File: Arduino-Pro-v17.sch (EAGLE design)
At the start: 39 parts, among them IC1 ATMEGA1281-16AU, IC2 MCP170312MB, J1 FTDI Basic Programmer

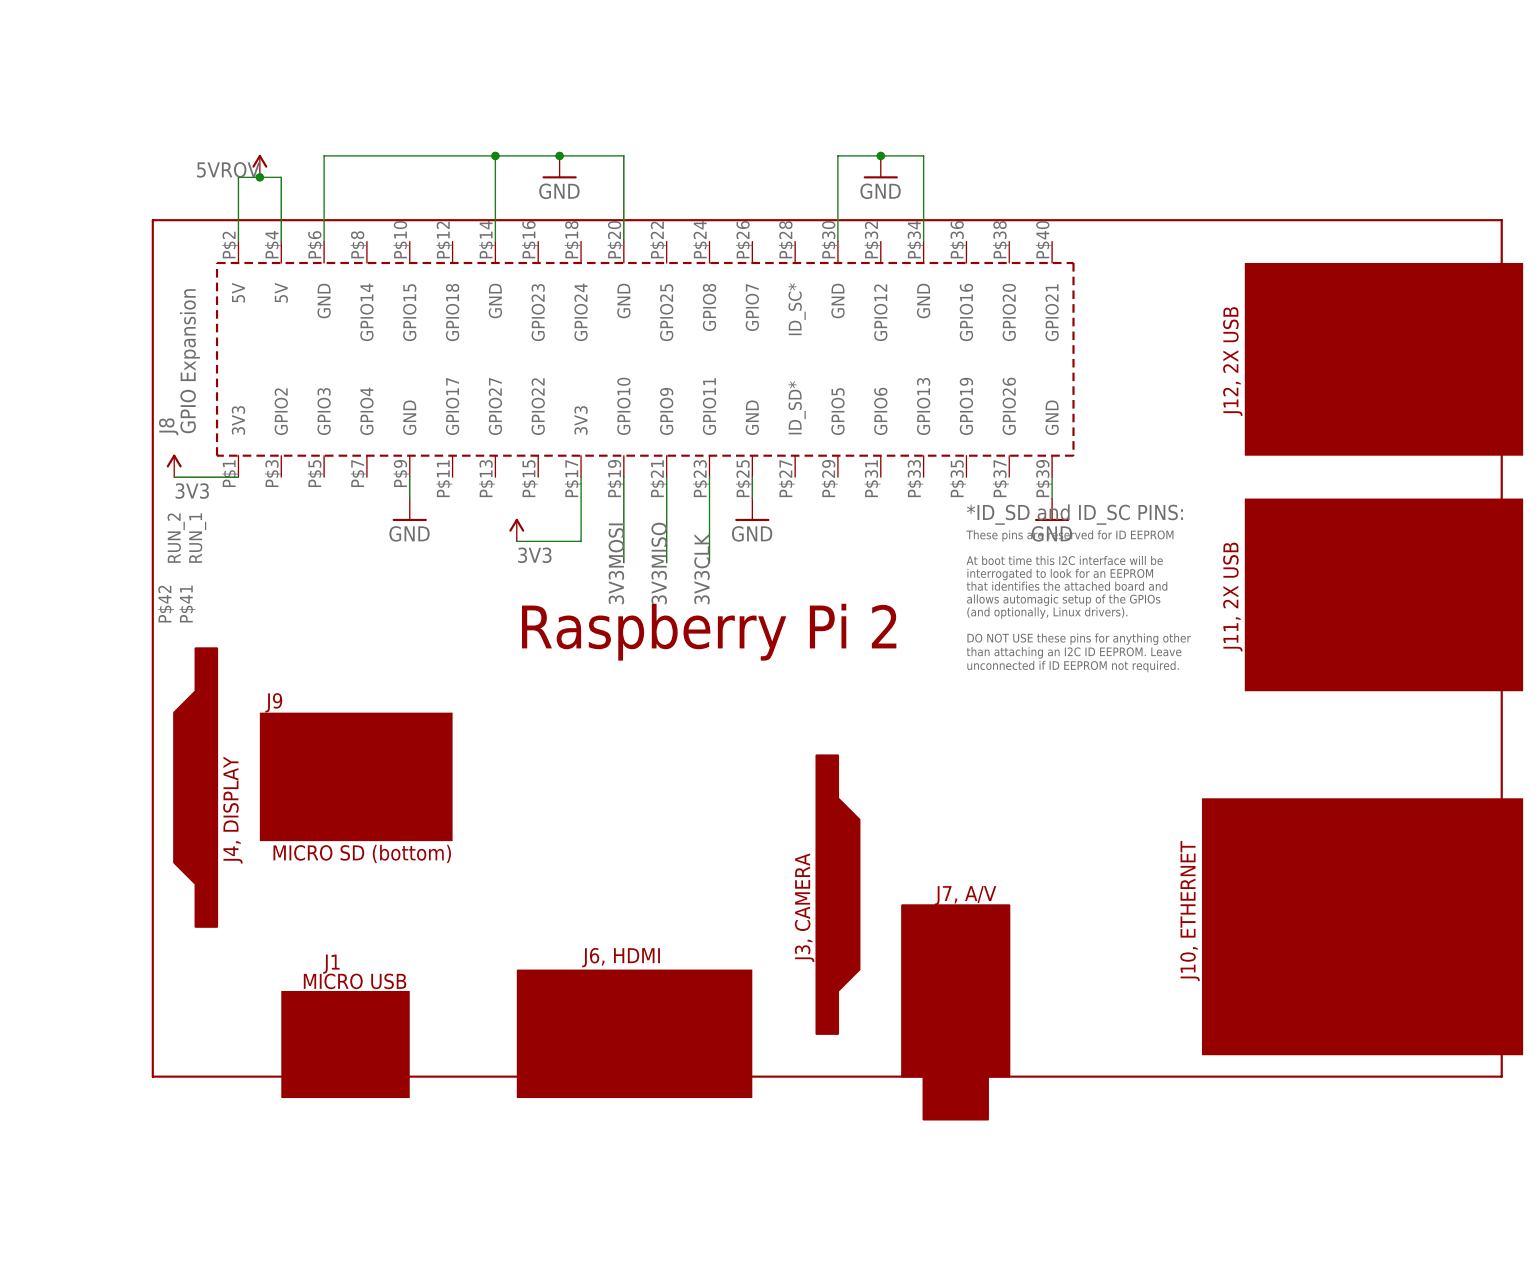
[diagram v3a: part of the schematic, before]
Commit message: Removed RPI board
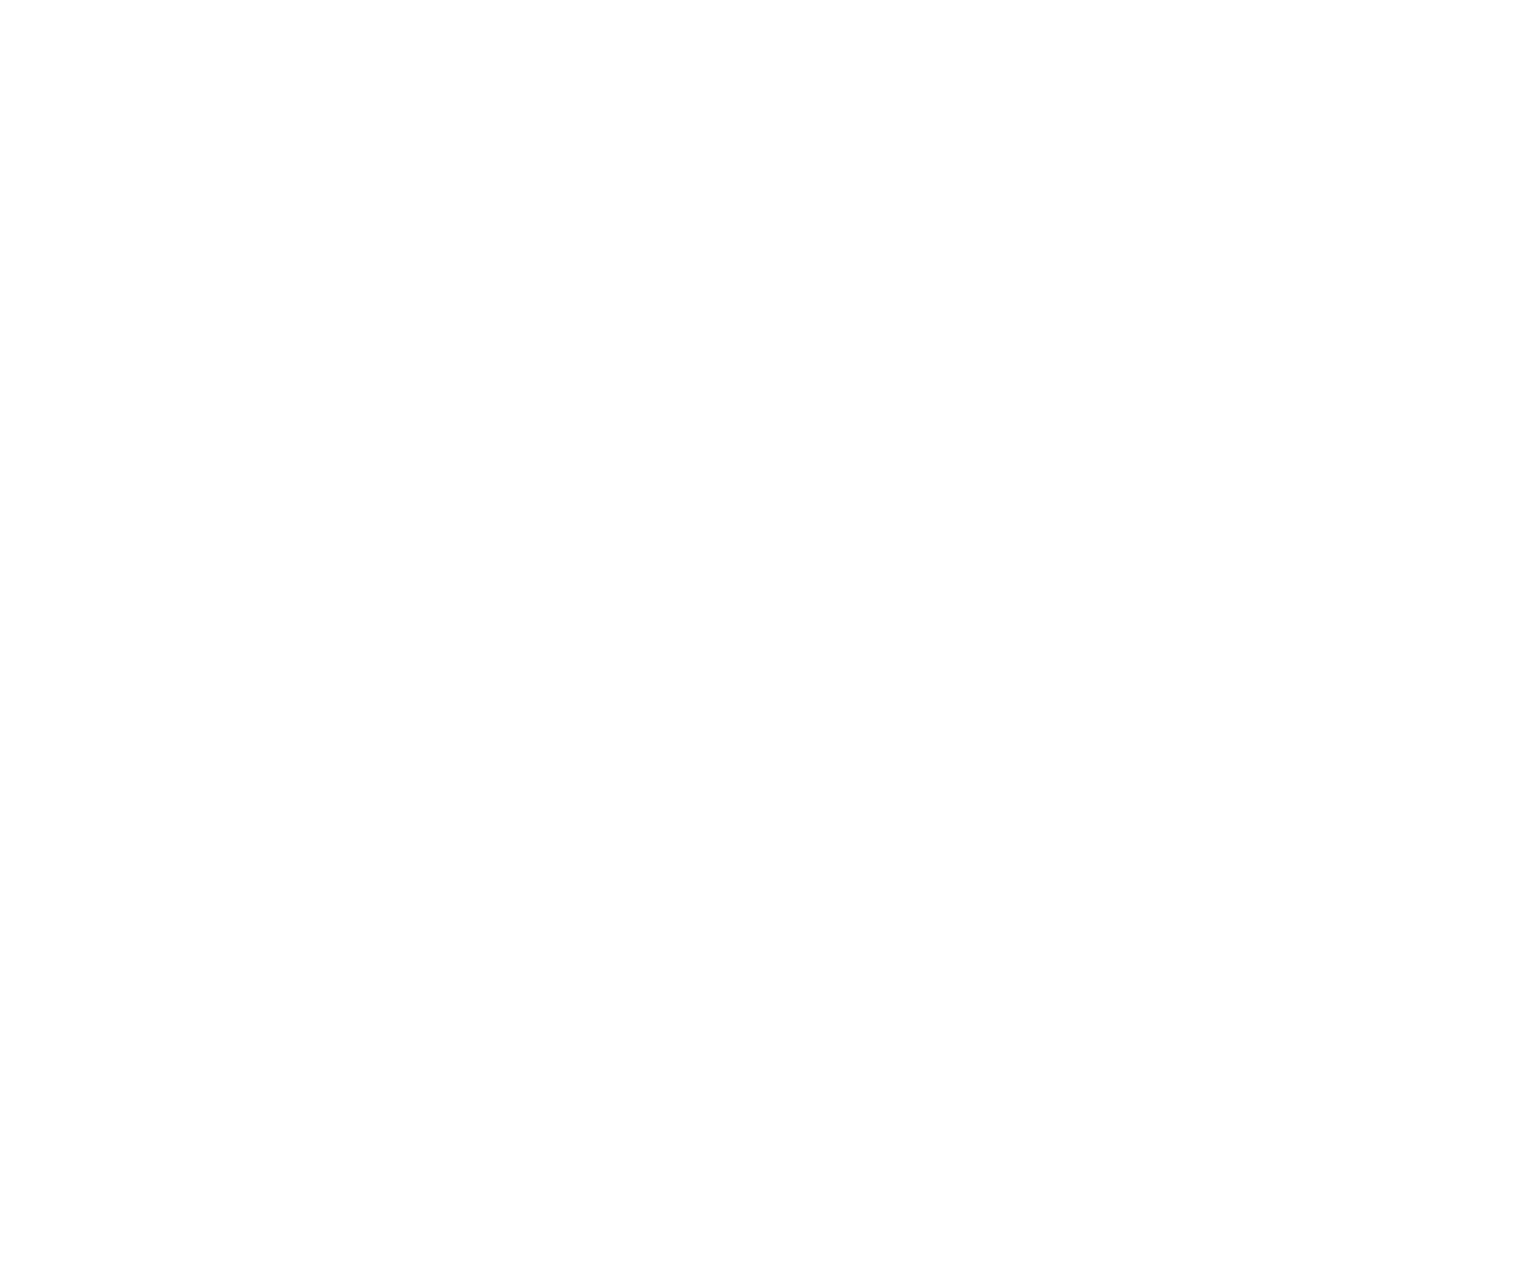
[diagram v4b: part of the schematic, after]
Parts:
- removed PCB1: RPI2, e14_Rpi2_RevA:RPI2
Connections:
- removed net 3V3CLK: PCB1.GPIO11
- removed net 3V3MISO: PCB1.GPIO9
- removed net 3V3MOSI: PCB1.GPIO10
- net 3V3: no longer PCB1.3V3@1, PCB1.3V3@17
- net 5VROV: no longer PCB1.5V@2, PCB1.5V@4
- net GND: no longer PCB1.GND@14, PCB1.GND@20, PCB1.GND@25, PCB1.GND@30, PCB1.GND@34, PCB1.GND@39, PCB1.GND@6, PCB1.GND@9
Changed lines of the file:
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@@
 <part name="P+8" library="SparkFun" deviceset="VCC" device=""/>
 <part name="FRAME2" library="SparkFun-Aesthetics" deviceset="FRAME-A4L" device=""/>
-<part name="PCB1" library="e14_Rpi2_RevA" deviceset="RPI2" device=""/>
 <part name="IC1" library="atmel-2005" deviceset="ATMEGA1281*" device="AU" technology="-16"/>
 <part name="C5" library="SparkFun" deviceset="CAP" device="0402-CAP" value="0.1uF"/>
@@
 <part name="GND13" library="SparkFun" deviceset="GND" device=""/>
 <part name="GND14" library="SparkFun" deviceset="GND" device=""/>
-<part name="GND15" library="SparkFun" deviceset="GND" device=""/>
-<part name="GND16" library="SparkFun" deviceset="GND" device=""/>
-<part name="GND17" library="SparkFun" deviceset="GND" device=""/>
-<part name="GND18" library="SparkFun" deviceset="GND" device=""/>
-<part name="GND19" library="SparkFun" deviceset="GND" device=""/>
-<part name="5VROV1" library="SparkFun-Aesthetics" deviceset="VCCA" device=""/>
 <part name="U$1" library="DiscreteComponents" deviceset="SWITCH" device=""/>
-<part name="3V1" library="SparkFun-Aesthetics" deviceset="VCCA" device=""/>
-<part name="3V4" library="SparkFun-Aesthetics" deviceset="VCCA" device=""/>
 <part name="J1" library="SparkFun-Connectors" deviceset="ARDUINO_SERIAL_PROGRAM" device="PTH" value="FTDI Basic Programmer"/>
 <part name="C4" library="SparkFun-Capacitors" deviceset="CAP" device="0603-CAP"/>
@@
 <instance part="P+8" gate="1" x="175.26" y="43.18"/>
 <instance part="FRAME2" gate="G$1" x="2.54" y="2.54"/>
-<instance part="PCB1" gate="G$1" x="299.72" y="55.88"/>
 <instance part="IC1" gate="G$1" x="-152.4" y="83.82"/>
 <instance part="C5" gate="G$1" x="-266.7" y="134.62" smashed="yes" rot="R180">
@@
 <instance part="GND13" gate="1" x="-91.44" y="81.28"/>
 <instance part="GND14" gate="1" x="-101.6" y="81.28"/>
-<instance part="GND15" gate="1" x="406.4" y="121.92"/>
-<instance part="GND16" gate="1" x="370.84" y="121.92"/>
-<instance part="GND17" gate="1" x="386.08" y="162.56"/>
-<instance part="GND18" gate="1" x="347.98" y="162.56"/>
-<instance part="GND19" gate="1" x="330.2" y="121.92"/>
-<instance part="5VROV1" gate="G$1" x="312.42" y="162.56" smashed="yes"/>
 <instance part="U$1" gate="G$1" x="-271.78" y="149.86" rot="R90"/>
-<instance part="3V1" gate="G$1" x="302.26" y="127" smashed="yes"/>
-<instance part="3V4" gate="G$1" x="342.9" y="119.38" smashed="yes"/>
 <instance part="J1" gate="G$1" x="137.16" y="137.16"/>
 <instance part="C4" gate="G$1" x="-284.48" y="160.02" rot="R270"/>
@@
 <pinref part="GND13" gate="1" pin="GND"/>
 <wire x1="-91.44" y1="86.36" x2="-91.44" y2="83.82" width="0.1524" layer="91"/>
-</segment>
-<segment>
-<pinref part="PCB1" gate="G$1" pin="GND@14"/>
-<wire x1="340.36" y1="154.94" x2="340.36" y2="165.1" width="0.1524" layer="91"/>
-<pinref part="GND18" gate="1" pin="GND"/>
-<wire x1="340.36" y1="165.1" x2="347.98" y2="165.1" width="0.1524" layer="91"/>
-<pinref part="PCB1" gate="G$1" pin="GND@20"/>
-<wire x1="347.98" y1="165.1" x2="355.6" y2="165.1" width="0.1524" layer="91"/>
-<wire x1="355.6" y1="165.1" x2="355.6" y2="154.94" width="0.1524" layer="91"/>
-<junction x="347.98" y="165.1"/>
-<pinref part="PCB1" gate="G$1" pin="GND@6"/>
-<wire x1="320.04" y1="154.94" x2="320.04" y2="165.1" width="0.1524" layer="91"/>
-<wire x1="320.04" y1="165.1" x2="340.36" y2="165.1" width="0.1524" layer="91"/>
-<junction x="340.36" y="165.1"/>
-</segment>
-<segment>
-<pinref part="PCB1" gate="G$1" pin="GND@30"/>
-<wire x1="381" y1="154.94" x2="381" y2="165.1" width="0.1524" layer="91"/>
-<pinref part="GND17" gate="1" pin="GND"/>
-<wire x1="381" y1="165.1" x2="386.08" y2="165.1" width="0.1524" layer="91"/>
-<pinref part="PCB1" gate="G$1" pin="GND@34"/>
-<wire x1="386.08" y1="165.1" x2="391.16" y2="165.1" width="0.1524" layer="91"/>
-<wire x1="391.16" y1="165.1" x2="391.16" y2="154.94" width="0.1524" layer="91"/>
-<junction x="386.08" y="165.1"/>
-</segment>
-<segment>
-<pinref part="PCB1" gate="G$1" pin="GND@25"/>
-<pinref part="GND16" gate="1" pin="GND"/>
-<wire x1="370.84" y1="127" x2="370.84" y2="124.46" width="0.1524" layer="91"/>
-</segment>
-<segment>
-<pinref part="PCB1" gate="G$1" pin="GND@39"/>
-<pinref part="GND15" gate="1" pin="GND"/>
-<wire x1="406.4" y1="127" x2="406.4" y2="124.46" width="0.1524" layer="91"/>
-</segment>
-<segment>
-<pinref part="PCB1" gate="G$1" pin="GND@9"/>
-<pinref part="GND19" gate="1" pin="GND"/>
-<wire x1="330.2" y1="127" x2="330.2" y2="124.46" width="0.1524" layer="91"/>
 </segment>
 <segment>
@@
 <net name="5VROV" class="0">
 <segment>
-<pinref part="PCB1" gate="G$1" pin="5V@2"/>
-<wire x1="309.88" y1="154.94" x2="309.88" y2="162.56" width="0.1524" layer="91"/>
-<pinref part="5VROV1" gate="G$1" pin="VCCA"/>
-<wire x1="309.88" y1="162.56" x2="312.42" y2="162.56" width="0.1524" layer="91"/>
-<pinref part="PCB1" gate="G$1" pin="5V@4"/>
-<wire x1="312.42" y1="162.56" x2="314.96" y2="162.56" width="0.1524" layer="91"/>
-<wire x1="314.96" y1="162.56" x2="314.96" y2="154.94" width="0.1524" layer="91"/>
-<junction x="312.42" y="162.56"/>
-<label x="304.8" y="162.56" size="1.778" layer="95"/>
-</segment>
-<segment>
 <pinref part="IC2" gate="G$1" pin="VI1"/>
 <wire x1="81.28" y1="149.86" x2="81.28" y2="154.94" width="0.1524" layer="91"/>
@@
 </net>
 <net name="3V3" class="0">
-<segment>
-<pinref part="3V1" gate="G$1" pin="VCCA"/>
-<pinref part="PCB1" gate="G$1" pin="3V3@1"/>
-<wire x1="302.26" y1="127" x2="309.88" y2="127" width="0.1524" layer="91"/>
-<label x="302.26" y="124.46" size="1.778" layer="95"/>
-</segment>
-<segment>
-<pinref part="3V4" gate="G$1" pin="VCCA"/>
-<pinref part="PCB1" gate="G$1" pin="3V3@17"/>
-<wire x1="342.9" y1="119.38" x2="350.52" y2="119.38" width="0.1524" layer="91"/>
-<wire x1="350.52" y1="119.38" x2="350.52" y2="127" width="0.1524" layer="91"/>
-<label x="342.9" y="116.84" size="1.778" layer="95"/>
-</segment>
 <segment>
 <pinref part="J1" gate="G$1" pin="VCC"/>
@@
 </segment>
 </net>
-<net name="3V3MOSI" class="0">
-<segment>
-<pinref part="PCB1" gate="G$1" pin="GPIO10"/>
-<wire x1="355.6" y1="127" x2="355.6" y2="116.84" width="0.1524" layer="91"/>
-<label x="355.6" y="111.76" size="1.778" layer="95" rot="R90"/>
-</segment>
-</net>
-<net name="3V3MISO" class="0">
-<segment>
-<pinref part="PCB1" gate="G$1" pin="GPIO9"/>
-<wire x1="360.68" y1="127" x2="360.68" y2="116.84" width="0.1524" layer="91"/>
-<label x="360.68" y="111.76" size="1.778" layer="95" rot="R90"/>
-</segment>
-</net>
-<net name="3V3CLK" class="0">
-<segment>
-<pinref part="PCB1" gate="G$1" pin="GPIO11"/>
-<wire x1="365.76" y1="127" x2="365.76" y2="116.84" width="0.1524" layer="91"/>
-<label x="365.76" y="111.76" size="1.778" layer="95" rot="R90"/>
-</segment>
-</net>
 <net name="JTTDI" class="0">
 <segment>
@@
 </schematic>
 </drawing>
-<compatibility>
-<note version="6.3" minversion="6.2.2" severity="warning">
-Since Version 6.2.2 text objects can contain more than one line,
-which will not be processed correctly with this version.
-</note>
-</compatibility>
 </eagle>

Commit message: Fixed some things with the board layout
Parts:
- added D2: 3.3V, SparkFun-DiscreteSemi:DIODE-ZENER3.3V
- J2: device SparkFun-Connectors:M02PTH -> SparkFun-Connectors:M03PTH
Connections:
- net 5VROV: now also J2.3; no longer J2.2
- net ALTVCC: now also D2.C
- net GND: now also D2.A, J2.2
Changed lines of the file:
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@@
 <?xml version="1.0" encoding="utf-8"?>
 <!DOCTYPE eagle SYSTEM "eagle.dtd">
-<eagle version="7.6.0">
+<eagle version="7.7.0">
 <drawing>
 <settings>
@@
 <part name="C4" library="SparkFun-Capacitors" deviceset="CAP" device="0603-CAP"/>
 <part name="IC2" library="linear" deviceset="MCP1703*" device="MB" technology="12"/>
-<part name="J2" library="SparkFun-Connectors" deviceset="M02" device="PTH"/>
+<part name="J2" library="SparkFun-Connectors" deviceset="M03" device="PTH"/>
 <part name="C6" library="SparkFun-Passives" deviceset="CAP" device="0603-CAP" value="10uF"/>
 <part name="C7" library="SparkFun-Passives" deviceset="CAP" device="0603-CAP" value="10uF"/>
@@
 <part name="SV1" library="con-lsta" deviceset="FE05-1" device=""/>
 <part name="JTAG_CONNECTOR" library="Connectors" deviceset="MICRO-FIT-4-SMD" device="" technology="-PART"/>
+<part name="D2" library="SparkFun-DiscreteSemi" deviceset="DIODE-ZENER" device="3.3V" value="3.3V"/>
 </parts>
 <sheets>
@@
 <instance part="C4" gate="G$1" x="-284.48" y="160.02" rot="R270"/>
 <instance part="IC2" gate="G$1" x="81.28" y="137.16" rot="R270"/>
-<instance part="J2" gate="G$1" x="43.18" y="116.84"/>
+<instance part="J2" gate="J$1" x="43.18" y="119.38"/>
 <instance part="C6" gate="G$1" x="-241.3" y="121.92"/>
 <instance part="C7" gate="G$1" x="-223.52" y="121.92"/>
@@
 <instance part="SV1" gate="G$1" x="-96.52" y="40.64" rot="R180"/>
 <instance part="JTAG_CONNECTOR" gate="G$1" x="-48.26" y="43.18" rot="R270"/>
+<instance part="D2" gate="G$1" x="63.5" y="119.38" rot="R270"/>
 </instances>
 <busses>
@@
 <pinref part="SV1" gate="G$1" pin="5"/>
 <wire x1="-104.14" y1="35.56" x2="-106.68" y2="35.56" width="0.1524" layer="91"/>
+</segment>
+<segment>
+<pinref part="J2" gate="J$1" pin="2"/>
+<label x="53.34" y="119.38" size="1.778" layer="95"/>
+<wire x1="50.8" y1="119.38" x2="60.96" y2="119.38" width="0.1524" layer="91"/>
+<wire x1="60.96" y1="119.38" x2="60.96" y2="121.92" width="0.1524" layer="91"/>
+<pinref part="D2" gate="G$1" pin="A"/>
+<wire x1="60.96" y1="121.92" x2="63.5" y2="121.92" width="0.1524" layer="91"/>
 </segment>
 </net>
@@
 </segment>
 <segment>
-<pinref part="J2" gate="G$1" pin="2"/>
-<wire x1="50.8" y1="119.38" x2="55.88" y2="119.38" width="0.1524" layer="91"/>
-<label x="53.34" y="119.38" size="1.778" layer="95"/>
+<pinref part="J2" gate="J$1" pin="3"/>
+<wire x1="50.8" y1="121.92" x2="55.88" y2="121.92" width="0.1524" layer="91"/>
+<label x="53.34" y="121.92" size="1.778" layer="95"/>
 </segment>
 </net>
@@
 <net name="ALTVCC" class="0">
 <segment>
+<label x="55.88" y="116.84" size="1.778" layer="95"/>
+<pinref part="J2" gate="J$1" pin="1"/>
+<pinref part="D2" gate="G$1" pin="C"/>
+<wire x1="50.8" y1="116.84" x2="63.5" y2="116.84" width="0.1524" layer="91"/>
 <pinref part="T1" gate="A" pin="D"/>
-<label x="55.88" y="116.84" size="1.778" layer="95"/>
-<pinref part="J2" gate="G$1" pin="1"/>
-<wire x1="50.8" y1="116.84" x2="66.04" y2="116.84" width="0.1524" layer="91"/>
-</segment>
-</net>
+<wire x1="63.5" y1="116.84" x2="66.04" y2="116.84" width="0.1524" layer="91"/>
+<junction x="63.5" y="116.84"/>
+</segment>
+</net>

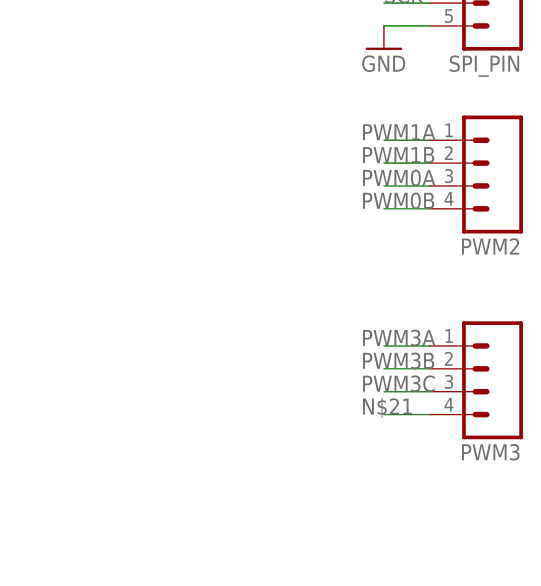
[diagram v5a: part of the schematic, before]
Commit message: Finished all routing, added pinouts for silkscreening on top of the board
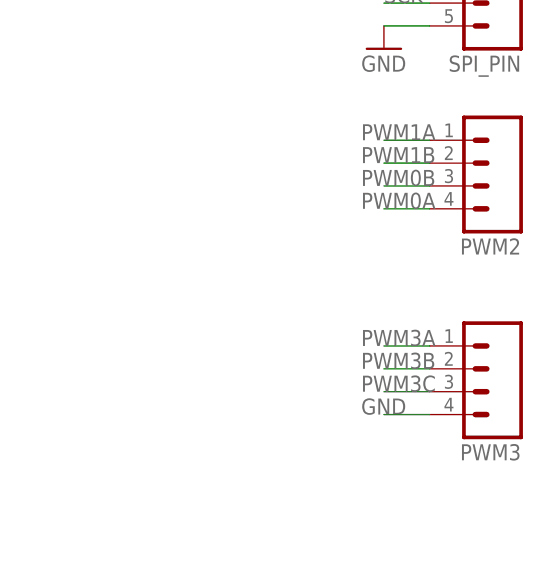
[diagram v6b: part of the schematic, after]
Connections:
- removed net N$21: PWM3.4
- net GND: now also PWM3.4
- net PWM0A: now also PWM2.4; no longer PWM2.3
- net PWM0B: now also PWM2.3; no longer PWM2.4
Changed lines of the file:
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@@
 <wire x1="60.96" y1="121.92" x2="63.5" y2="121.92" width="0.1524" layer="91"/>
+</segment>
+<segment>
+<pinref part="PWM3" gate="G$1" pin="4"/>
+<wire x1="218.44" y1="86.36" x2="213.36" y2="86.36" width="0.1524" layer="91"/>
+<label x="210.82" y="86.36" size="1.778" layer="95"/>
 </segment>
 </net>
@@
 </segment>
 </net>
-<net name="N$21" class="0">
-<segment>
-<pinref part="PWM3" gate="G$1" pin="4"/>
-<wire x1="218.44" y1="86.36" x2="213.36" y2="86.36" width="0.1524" layer="91"/>
-<label x="210.82" y="86.36" size="1.778" layer="95"/>
-</segment>
-</net>
 <net name="PWM0B" class="0">
 <segment>
@@
 </segment>
 <segment>
+<pinref part="PWM2" gate="G$1" pin="3"/>
+<wire x1="218.44" y1="111.76" x2="213.36" y2="111.76" width="0.1524" layer="91"/>
+<label x="210.82" y="111.76" size="1.778" layer="95"/>
+</segment>
+</net>
+<net name="PWM0A" class="0">
+<segment>
+<pinref part="IC1" gate="G$1" pin="(OC0A/OC1C/PCINT7)PB7"/>
+<wire x1="-116.84" y1="137.16" x2="-109.22" y2="137.16" width="0.1524" layer="91"/>
+<label x="-114.3" y="137.16" size="1.778" layer="95"/>
+</segment>
+<segment>
 <pinref part="PWM2" gate="G$1" pin="4"/>
 <wire x1="218.44" y1="109.22" x2="213.36" y2="109.22" width="0.1524" layer="91"/>
@@
 </segment>
 </net>
-<net name="PWM0A" class="0">
-<segment>
-<pinref part="IC1" gate="G$1" pin="(OC0A/OC1C/PCINT7)PB7"/>
-<wire x1="-116.84" y1="137.16" x2="-109.22" y2="137.16" width="0.1524" layer="91"/>
-<label x="-114.3" y="137.16" size="1.778" layer="95"/>
-</segment>
-<segment>
-<pinref part="PWM2" gate="G$1" pin="3"/>
-<wire x1="218.44" y1="111.76" x2="213.36" y2="111.76" width="0.1524" layer="91"/>
-<label x="210.82" y="111.76" size="1.778" layer="95"/>
-</segment>
-</net>
